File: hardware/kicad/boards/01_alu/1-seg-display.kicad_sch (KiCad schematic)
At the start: 13 parts, among them U191 HDSP-A153, U192 74LS377, U193 74AHC541

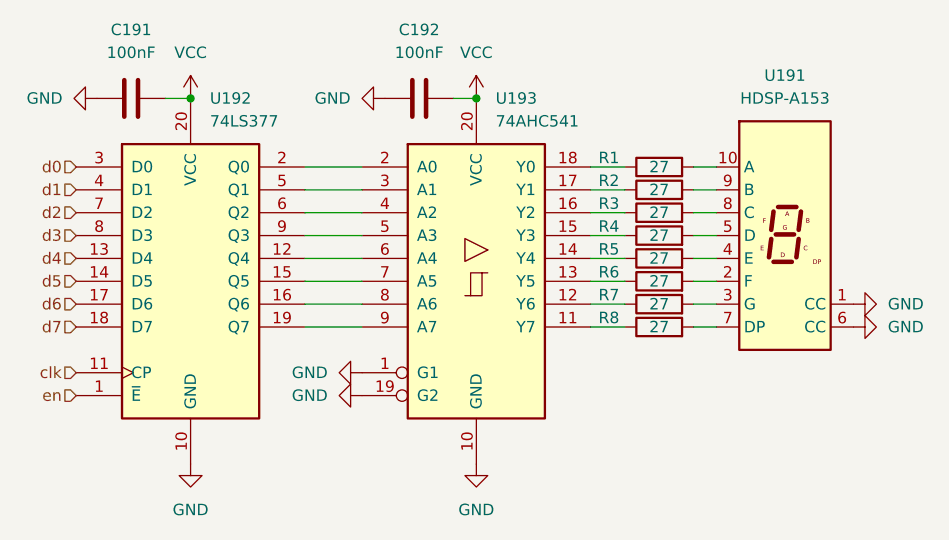
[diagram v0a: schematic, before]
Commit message: kicad: checkpoint; designed the alu display logic; clock circuit
Added registers for each display to ensure robustness and less worry about debugging screen, keeping focus on the alu board and other components
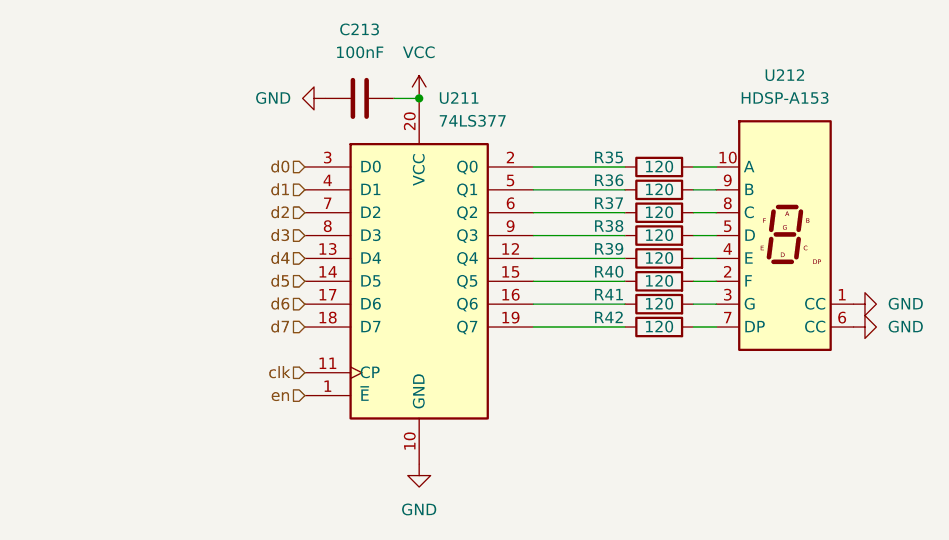
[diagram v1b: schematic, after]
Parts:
- removed C192: 100nF, Capacitor_SMD:C_0805_2012Metric, symbol Device:C
- removed R2, R3, R4, R5, R6, R7, R8: 27, Resistor_SMD:R_0805_2012Metric, symbol Device:R
- removed U193: 74AHC541, Package_SO:SOIC-20W_7.5x12.8mm_P1.27mm, symbol 74xx:74AHC541
- added R36, R37, R38, R39, R40, R41, R42: 120, Resistor_SMD:R_0805_2012Metric, symbol Device:R
- R35: renamed from R1; value 27 -> 120
- renumbered C191 to C213, U192 to U211, U191 to U212
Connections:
- net at U212.9 (B): now also R36.2
- net at U211.12 (Q4): now also R39.1
- net at U211.15 (Q5): now also R40.1
- net at U211.16 (Q6): now also R41.1
- net at U211.19 (Q7): now also R42.1
- net at U211.2 (Q0): now also R35.1
- net at U211.5 (Q1): now also R36.1
- net at U211.6 (Q2): now also R37.1
- net at U211.9 (Q3): now also R38.1
- net at U212.5 (D): now also R38.2
- net at U212.2 (F): now also R40.2
- net at U212.3 (G): now also R41.2
- net at U212.4 (E): now also R39.2
- net at U212.7 (DP): now also R42.2
- net at U212.8 (C): now also R37.2
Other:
- moved on the sheet: C213, U211

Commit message: alu: completed all core schematics; DRC and ERC pending 🎉
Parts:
- renumbered C213 to C173, U211 to U173, U212 to U174

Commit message: refactor: improved global labeling and reduced ERC from 300+ to 6 power flags and minor connector in errors
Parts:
- renumbered C173 to C179, R35 to R33, R36 to R34, R37 to R35, R38 to R36, R39 to R37, R40 to R38, R41 to R39, R42 to R40, U173 to U179, U174 to U180
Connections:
- net clk renamed textclk
- net d0 renamed d-text0
- net d1 renamed d-text1
- net d2 renamed d-text2
- net d3 renamed d-text3
- net d4 renamed d-text4
- net d5 renamed d-text5
- net d6 renamed d-text6
- net d7 renamed d-text7

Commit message: fix: fixed erc to 0; remaining are warnings about labeling which are being fixed; latest alu schematics pending decoration and organization
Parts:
- renumbered C179 to C194, U179 to U194, U180 to U195

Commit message: refactor: placing buses in design across alu to improve readability and debugging
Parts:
- renumbered C194 to C216, U194 to U216, U195 to U217

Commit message: feat: designed ALU board with 0 ERC errors or warnings 🎉
Final review of logical correctness and footprints and then routing begins
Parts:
- renumbered C216 to C7901, R33 to R7901, R34 to R7902, R35 to R7903, R36 to R7904, R37 to R7905, R38 to R7906, R39 to R7907, R40 to R7908, U217 to U7901, U216 to U7902

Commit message: arch: added LEDs, override switches; fixed errors and warnings to 0
ready for routing after logical coherence check
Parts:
- renumbered C7901 to C233, R7901 to R15, R7902 to R16, R7903 to R17, R7904 to R18, R7905 to R19, R7906 to R20, R7907 to R21, R7908 to R22, U7902 to U233, U7901 to U234

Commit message: fix: fixed the zero flag detection logic
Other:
- title: (none) -> Tomato32 ALU
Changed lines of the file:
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@@
 	(generator_version "10.0")
 	(paper "A4")
+	(title_block
+		(title "Tomato32 ALU")
+		(date "2026-06-23")
+		(rev "v1.0")
+	)
 	(junction
 		(at 91.44 67.31)
